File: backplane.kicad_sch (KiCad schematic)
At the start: 11 parts, among them J5 Edge_Conn_HSEC8-120, U12 ESD204DQAR, U13 ESD204DQAR, U14 ESD204DQAR, U15 ESD204DQAR, U16 ESD204DQAR, U17 ESD204DQAR, U46 MP8869S, U47 TPS56C230, U48 AP62301_TSOT, U49 AP62301_TSOT

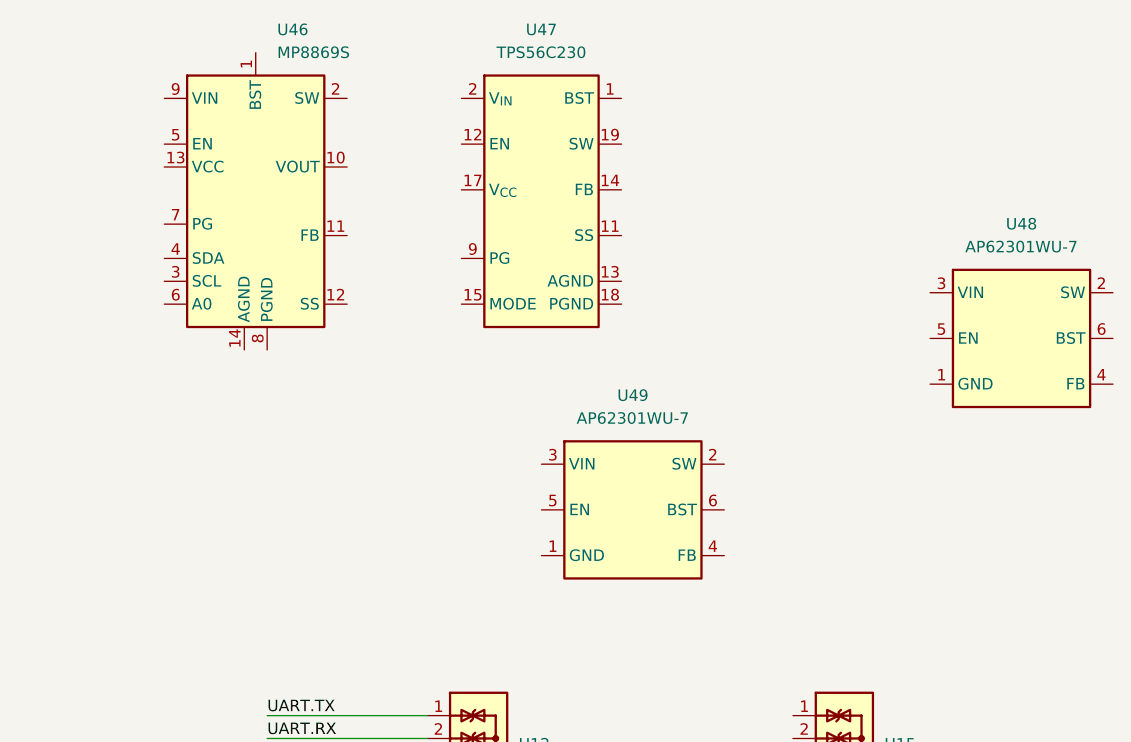
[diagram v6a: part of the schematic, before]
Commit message: [#58137] Add DC/DC supplies
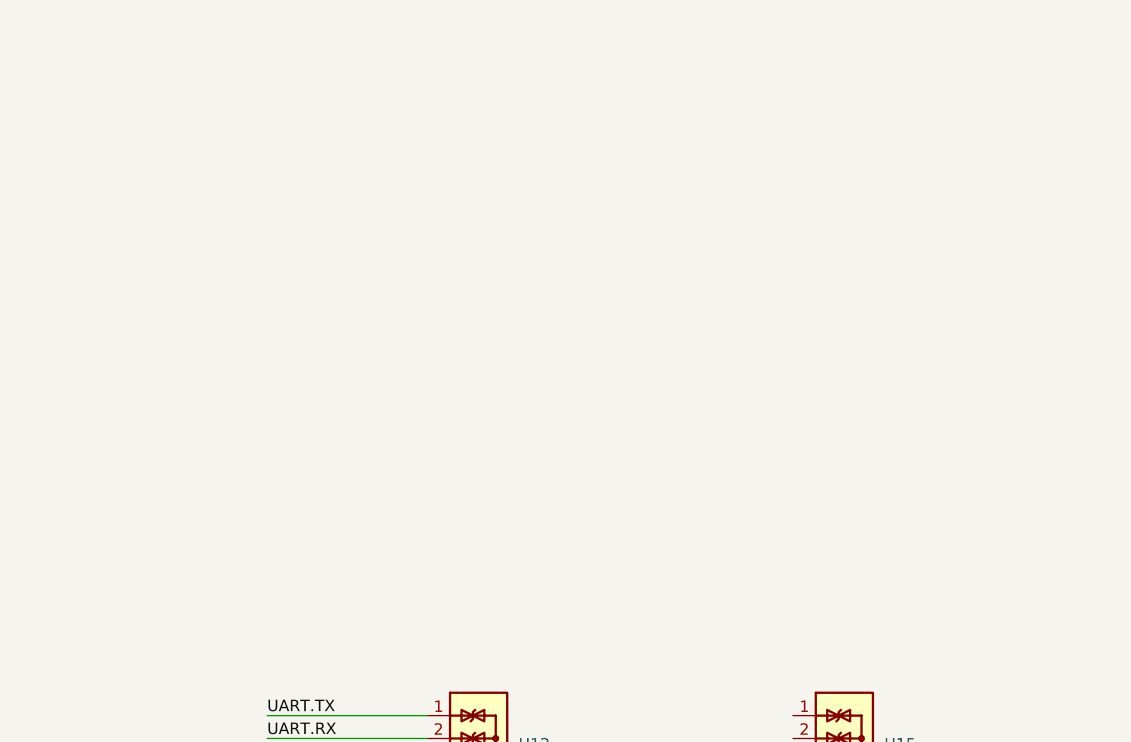
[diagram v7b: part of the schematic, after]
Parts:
- removed U46: MP8869S, antmicro-footprints:MPS_QFN-14_MP8869S, symbol antmicroPMICVoltageRegulatorsDCDCSwitchingRegulators:MP8869S
- removed U47: TPS56C230, antmicro-footprints:QFN-20-1EP_3x3mm_P0.45mm, symbol antmicroDCDCConverters:TPS56C230
- removed U48, U49: AP62301_TSOT, antmicro-footprints:TSOT23-6, symbol antmicroDCDCConverters:AP62301_TSOT
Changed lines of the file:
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@@
-    )
-  )
-  (symbol (lib_id "antmicroDCDCConverters:AP62301_TSOT") (at 332.74 102.87 0) (unit 1)
-    (in_bom yes) (on_board yes) (dnp no) (fields_autoplaced)
-    (property "Reference" "U48" (at 342.9 95.25 0)
-      (effects (font (size 1.27 1.27) (thickness 0.15)))
-    )
-    (property "Value" "AP62301_TSOT" (at 368.3 110.49 0)
-      (effects (font (size 1.27 1.27) (thickness 0.15)) (justify left bottom) hide)
-    )
-    (property "Footprint" "antmicro-footprints:TSOT23-6" (at 368.3 113.03 0)
-      (effects (font (size 1.27 1.27) (thickness 0.15)) (justify left bottom) hide)
-    )
-    (property "Datasheet" "https://www.diodes.com/assets/Datasheets/AP62300_AP62301_AP62300T.pdf" (at 368.3 115.57 0)
-      (effects (font (size 1.27 1.27) (thickness 0.15)) (justify left bottom) hide)
-    )
-    (property "MPN" "AP62301WU-7" (at 342.9 97.79 0)
-      (effects (font (size 1.27 1.27) (thickness 0.15)))
-    )
-    (property "Manufacturer" "Diodes Incorporated" (at 368.3 118.11 0)
-      (effects (font (size 1.27 1.27) (thickness 0.15)) (justify left bottom) hide)
-    )
-    (property "Author" "Antmicro" (at 368.3 120.65 0)
-      (effects (font (size 1.27 1.27) (thickness 0.15)) (justify left bottom) hide)
-    )
-    (property "License" "Apache-2.0" (at 368.3 123.19 0)
-      (effects (font (size 1.27 1.27) (thickness 0.15)) (justify left bottom) hide)
-    )
-    (pin "2")
-    (pin "4")
-    (pin "3")
-    (pin "1")
-    (pin "5")
-    (pin "6")
-    (instances
-      (project "com-express-7-baseboard"
-        (path "/1b8c34da-dad5-4b0b-8c4b-45db766c4dfa/55405a83-d274-4fdb-aba5-7f854fcb14c7"
-          (reference "U48") (unit 1)
-        )
-      )
     )
   )
@@
     )
   )
-  (symbol (lib_id "antmicroDCDCConverters:AP62301_TSOT") (at 289.56 121.92 0) (unit 1)
-    (in_bom yes) (on_board yes) (dnp no) (fields_autoplaced)
-    (property "Reference" "U49" (at 299.72 114.3 0)
-      (effects (font (size 1.27 1.27) (thickness 0.15)))
-    )
-    (property "Value" "AP62301_TSOT" (at 325.12 129.54 0)
-      (effects (font (size 1.27 1.27) (thickness 0.15)) (justify left bottom) hide)
-    )
-    (property "Footprint" "antmicro-footprints:TSOT23-6" (at 325.12 132.08 0)
-      (effects (font (size 1.27 1.27) (thickness 0.15)) (justify left bottom) hide)
-    )
-    (property "Datasheet" "https://www.diodes.com/assets/Datasheets/AP62300_AP62301_AP62300T.pdf" (at 325.12 134.62 0)
-      (effects (font (size 1.27 1.27) (thickness 0.15)) (justify left bottom) hide)
-    )
-    (property "MPN" "AP62301WU-7" (at 299.72 116.84 0)
-      (effects (font (size 1.27 1.27) (thickness 0.15)))
-    )
-    (property "Manufacturer" "Diodes Incorporated" (at 325.12 137.16 0)
-      (effects (font (size 1.27 1.27) (thickness 0.15)) (justify left bottom) hide)
-    )
-    (property "Author" "Antmicro" (at 325.12 139.7 0)
-      (effects (font (size 1.27 1.27) (thickness 0.15)) (justify left bottom) hide)
-    )
-    (property "License" "Apache-2.0" (at 325.12 142.24 0)
-      (effects (font (size 1.27 1.27) (thickness 0.15)) (justify left bottom) hide)
-    )
-    (pin "2")
-    (pin "3")
-    (pin "1")
-    (pin "6")
-    (pin "4")
-    (pin "5")
-    (instances
-      (project "com-express-7-baseboard"
-        (path "/1b8c34da-dad5-4b0b-8c4b-45db766c4dfa/55405a83-d274-4fdb-aba5-7f854fcb14c7"
-          (reference "U49") (unit 1)
-        )
-      )
-    )
-  )
   (symbol (lib_id "antmicroTVSDiodes:ESD204DQAR") (at 317.5 180.34 0) (unit 1)
     (in_bom yes) (on_board yes) (dnp no) (fields_autoplaced)
@@
     )
   )
-  (symbol (lib_id "antmicroPMICVoltageRegulatorsDCDCSwitchingRegulators:MP8869S") (at 257.81 76.2 0) (unit 1)
-    (in_bom yes) (on_board yes) (dnp no) (fields_autoplaced)
-    (property "Reference" "U46" (at 260.183 73.66 0)
-      (effects (font (size 1.27 1.27) (thickness 0.15)) (justify left))
-    )
-    (property "Value" "MP8869S" (at 260.183 76.2 0)
-      (effects (font (size 1.27 1.27) (thickness 0.15)) (justify left))
-    )
-    (property "Footprint" "antmicro-footprints:MPS_QFN-14_MP8869S" (at 283.21 87.63 0)
-      (effects (font (size 1.27 1.27) (thickness 0.15)) (justify left bottom) hide)
-    )
-    (property "Datasheet" "https://www.mouser.com/datasheet/2/277/MP8869S-2946178.pdf" (at 283.21 90.17 0)
-      (effects (font (size 1.27 1.27) (thickness 0.15)) (justify left bottom) hide)
-    )
-    (property "MPN" "MP8869SGL-P" (at 283.21 92.71 0)
-      (effects (font (size 1.27 1.27) (thickness 0.15)) (justify left bottom) hide)
-    )
-    (property "Manufacturer" "Monolithic Power Systems" (at 283.21 95.25 0)
-      (effects (font (size 1.27 1.27) (thickness 0.15)) (justify left bottom) hide)
-    )
-    (property "Author" "Antmicro" (at 283.21 97.79 0)
-      (effects (font (size 1.27 1.27) (thickness 0.15)) (justify left bottom) hide)
-    )
-    (property "License" "Apache-2.0" (at 283.21 100.33 0)
-      (effects (font (size 1.27 1.27) (thickness 0.15)) (justify left bottom) hide)
-    )
-    (pin "4")
-    (pin "8")
-    (pin "6")
-    (pin "9")
-    (pin "11")
-    (pin "2")
-    (pin "7")
-    (pin "12")
-    (pin "5")
-    (pin "1")
-    (pin "13")
-    (pin "10")
-    (pin "3")
-    (pin "14")
-    (instances
-      (project "com-express-7-baseboard"
-        (path "/1b8c34da-dad5-4b0b-8c4b-45db766c4dfa/55405a83-d274-4fdb-aba5-7f854fcb14c7"
-          (reference "U46") (unit 1)
-        )
-      )
-    )
-  )
   (symbol (lib_id "antmicroTVSDiodes:ESD204DQAR") (at 317.5 149.86 0) (unit 1)
     (in_bom yes) (on_board yes) (dnp no) (fields_autoplaced)
@@
         )
       )
-    )
-  )
-  (symbol (lib_id "antmicroDCDCConverters:TPS56C230") (at 280.67 81.28 0) (unit 1)
-    (in_bom yes) (on_board yes) (dnp no) (fields_autoplaced)
-    (property "Reference" "U47" (at 289.56 73.66 0)
-      (effects (font (size 1.27 1.27) (thickness 0.15)))
-    )
-    (property "Value" "TPS56C230" (at 289.56 76.2 0)
-      (effects (font (size 1.27 1.27) (thickness 0.15)))
-    )
-    (property "Footprint" "antmicro-footprints:QFN-20-1EP_3x3mm_P0.45mm" (at 313.69 88.9 0)
-      (effects (font (size 1.27 1.27) (thickness 0.15)) (justify left bottom) hide)
-    )
-    (property "Datasheet" "https://www.ti.com/lit/ds/symlink/tps56c230.pdf?ts=1672843259715&ref_url=https%253A%252F%252Fwww.ti.com%252Fproduct%252FTPS56C230" (at 313.69 91.44 0)
-      (effects (font (size 1.27 1.27) (thickness 0.15)) (justify left bottom) hide)
-    )
-    (property "Manufacturer" "Texas Instruments" (at 313.69 93.98 0)
-      (effects (font (size 1.27 1.27) (thickness 0.15)) (justify left bottom) hide)
-    )
-    (property "MPN" "TPS56C230RJER" (at 313.69 96.52 0)
-      (effects (font (size 1.27 1.27) (thickness 0.15)) (justify left bottom) hide)
-    )
-    (property "Author" "Antmicro" (at 313.69 99.06 0)
-      (effects (font (size 1.27 1.27) (thickness 0.15)) (justify left bottom) hide)
-    )
-    (property "License" "Apache-2.0" (at 313.69 101.6 0)
-      (effects (font (size 1.27 1.27) (thickness 0.15)) (justify left bottom) hide)
-    )
-    (pin "12")
-    (pin "11")
-    (pin "14")
-    (pin "10")
-    (pin "18")
-    (pin "6")
-    (pin "4")
-    (pin "16")
-    (pin "3")
-    (pin "17")
-    (pin "5")
-    (pin "9")
-    (pin "8")
-    (pin "7")
-    (pin "21")
-    (pin "1")
-    (pin "2")
-    (pin "19")
-    (pin "20")
-    (pin "13")
-    (pin "15")
-    (instances
-      (project "com-express-7-baseboard"
-        (path "/1b8c34da-dad5-4b0b-8c4b-45db766c4dfa/55405a83-d274-4fdb-aba5-7f854fcb14c7"
-          (reference "U47") (unit 1)
-        )
-      )

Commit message: Fix ERC
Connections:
- no-connect marks 0 -> 2
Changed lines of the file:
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@@
   (junction (at 275.59 175.26) (diameter 0) (color 0 0 0 0)
   )
+  (junction (at 190.5 121.92) (diameter 0) (color 0 0 0 0)
+  )
   (junction (at 190.5 120.65) (diameter 0) (color 0 0 0 0)
   )
@@
   (junction (at 204.47 157.48) (diameter 0) (color 0 0 0 0)
   )
+  (no_connect (at 317.5 152.4))
+  (no_connect (at 317.5 149.86))
   (bus_entry (at 175.26 167.64) (size -1.27 1.27)
     (stroke (width 0) (type default))
@@
     (stroke (width 0) (type default))
   )
-  (wire (pts (xy 190.5 120.65) (xy 190.5 124.46))
+  (wire (pts (xy 190.5 120.65) (xy 190.5 121.92))
     (stroke (width 0) (type default))
   )
@@
     (stroke (width 0) (type default))
   )
+  (wire (pts (xy 205.74 187.96) (xy 207.01 187.96))
+    (stroke (width 0) (type default))
+  )
   (wire (pts (xy 259.08 157.48) (xy 276.86 157.48))
     (stroke (width 0) (type default))
@@
     (stroke (width 0) (type default))
   )
+  (wire (pts (xy 205.74 189.23) (xy 205.74 187.96))
+    (stroke (width 0) (type default))
+  )
   (wire (pts (xy 303.53 157.48) (xy 317.5 157.48))
     (stroke (width 0) (type default))
@@
   )
   (bus (pts (xy 176.53 173.99) (xy 176.53 176.53))
+    (stroke (width 0) (type default))
+  )
+  (wire (pts (xy 190.5 121.92) (xy 190.5 124.46))
     (stroke (width 0) (type default))
   )
@@
     )
   )
+  (symbol (lib_id "antmicropower:PWR_FLAG") (at 207.01 187.96 270) (unit 1)
+    (in_bom yes) (on_board yes) (dnp no) (fields_autoplaced)
+    (property "Reference" "#FLG08" (at 208.915 187.96 0)
+      (effects (font (size 1.27 1.27)) hide)
+    )
+    (property "Value" "PWR_FLAG" (at 210.82 187.9599 90)
+      (effects (font (size 1.27 1.27)) (justify left))
+    )
+    (property "Footprint" "" (at 207.01 187.96 0)
+      (effects (font (size 1.27 1.27)) hide)
+    )
+    (property "Datasheet" "" (at 207.01 187.96 0)
+      (effects (font (size 1.27 1.27)) hide)
+    )
+    (pin "1")
+    (instances
+      (project "com-express-7-baseboard"
+        (path "/1b8c34da-dad5-4b0b-8c4b-45db766c4dfa/55405a83-d274-4fdb-aba5-7f854fcb14c7"
+          (reference "#FLG08") (unit 1)
+        )
+      )
+    )
+  )
   (symbol (lib_id "antmicroTVSDiodes:ESD204DQAR") (at 317.5 165.1 0) (unit 1)
     (in_bom yes) (on_board yes) (dnp no) (fields_autoplaced)
@@
         )
       )
+    )
+  )
+  (symbol (lib_id "antmicropower:GND") (at 205.74 189.23 0) (unit 1)
+    (in_bom yes) (on_board yes) (dnp no)
+    (property "Reference" "#PWR0433" (at 214.63 191.77 0)
+      (effects (font (size 1.27 1.27) (thickness 0.15)) (justify left bottom) hide)
+    )
+    (property "Value" "GND" (at 205.74 193.04 0)
+      (effects (font (size 1.27 1.27) (thickness 0.15)))
+    )
+    (property "Footprint" "" (at 214.63 196.85 0)
+      (effects (font (size 1.27 1.27) (thickness 0.15)) (justify left bottom) hide)
+    )
+    (property "Datasheet" "" (at 214.63 201.93 0)
+      (effects (font (size 1.27 1.27) (thickness 0.15)) (justify left bottom) hide)
+    )
+    (property "Author" "Antmicro" (at 214.63 196.85 0)
+      (effects (font (size 1.27 1.27) (thickness 0.15)) (justify left bottom) hide)
+    )
+    (property "License" "Apache-2.0" (at 214.63 199.39 0)
+      (effects (font (size 1.27 1.27) (thickness 0.15)) (justify left bottom) hide)
+    )
+    (pin "1")
+    (instances
+      (project "com-express-7-baseboard"
+        (path "/1b8c34da-dad5-4b0b-8c4b-45db766c4dfa/55405a83-d274-4fdb-aba5-7f854fcb14c7"
+          (reference "#PWR0433") (unit 1)
+        )
+      )
+    )
+  )
+  (symbol (lib_id "antmicropower:PWR_FLAG") (at 190.5 121.92 90) (unit 1)
+    (in_bom yes) (on_board yes) (dnp no)
+    (property "Reference" "#FLG014" (at 188.595 121.92 0)
+      (effects (font (size 1.27 1.27)) hide)
+    )
+    (property "Value" "PWR_FLAG" (at 186.69 121.92 0)
+      (effects (font (size 1.27 1.27)) hide)
+    )
+    (property "Footprint" "" (at 190.5 121.92 0)
+      (effects (font (size 1.27 1.27)) hide)
+    )
+    (property "Datasheet" "" (at 190.5 121.92 0)
+      (effects (font (size 1.27 1.27)) hide)
+    )
+    (pin "1")
+    (instances
+      (project "com-express-7-baseboard"
+        (path "/1b8c34da-dad5-4b0b-8c4b-45db766c4dfa/55405a83-d274-4fdb-aba5-7f854fcb14c7"
+          (reference "#FLG014") (unit 1)
+        )
+      )
